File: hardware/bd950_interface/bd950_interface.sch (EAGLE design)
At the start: 16 parts, among them IC1 FT4232HL, IC2 MAX208ECWG, IC3 4050D, X1 ECG.0B.304.CLV

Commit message: Continue work on BD950 interface board
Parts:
- added C1, C2, C3: 3.3uF, resistor:C-USC0603
- added IC4: AT93C46A-10SQ-2.7, atmel:AT93C46A-10SQ-2.7
- added Q1: (no value), adafruit:CRYSTALHC49S
- added R10: 2.2k, resistor:R-US_R0603
- added R11, R6: 12k, resistor:R-US_R0603
- added R7, R8, R9: 10k, resistor:R-US_R0603
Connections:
- new net +3V3: IC1CORE.VCCIO@1, IC1CORE.VCCIO@2, IC1CORE.VCCIO@3, IC1CORE.VCCIO@4, IC1CORE.VPHY, IC1CORE.VPLL, IC1CORE.VREGIN, IC4.VCC, R11.2, R7.2, R8.2, R9.2
- new net EECLK: IC1CORE.EECLK, IC4.SK, R8.1
- new net EECS: IC1CORE.EECS, IC4.CS, R9.1
- new net EEDATA: IC1CORE.EEDATA, IC4.DI, R10.2
- new net N$10: C1.1, IC1CORE.VCORE@1, IC1CORE.VCORE@2, IC1CORE.VCORE@3, IC1CORE.VREGOUT
- new net N$11: C3.1, IC1CORE.XTOUT, Q1.1
- new net N$12: C2.1, IC1CORE.XTIN, Q1.2
- new net N$13: IC1CORE.RESET#, R11.1
- new net N$6: IC1CORE.REF, R6.2
- new net N$9: IC4.DO, R10.1, R7.1
- new net UART1_RXD: IC1A.DB1/RXD, IC2G$1.R1OUT
- new net UART1_TXD: IC1A.DB0/TXD, IC2G$1.T1IN
- new net UART2_RXD: IC1B.DB1/RXD, IC2G$1.R2OUT
- new net UART2_TXD: IC1B.DB0/TXD, IC2G$1.T2IN
- new net UART3_RXD: IC2G$1.R3OUT
- new net UART3_TXD: IC1C.DB0/TXD, IC1C.DB1/RXD, IC2G$1.T3IN
- new net UART4_RXD: IC1D.DB1/RXD, IC2G$1.R4OUT, IC2G$1.T4IN
- new net UART4_TXD: IC1D.DB0/TXD
- net 1PPS_PORT1: now also IC1A.DB6/DCD
- net 1PPS_PORT2: now also IC1B.DB6/DCD
- net 1PPS_PORT3: now also IC1C.DB6/DCD
- net 1PPS_PORT4: now also IC1D.DB6/DCD
- net GND: now also C1.2, C2.2, C3.2, IC1CORE.TEST, IC4.GND, R6.1
- net PORT1_RXD: now also IC2G$1.T1OUT
- net PORT2_RXD: now also IC2G$1.T2OUT
- net PORT3_RXD: now also IC2G$1.T3OUT
- net PORT4_RXD: now also IC2G$1.T4OUT
- net PORT4_TXD: now also IC2G$1.R1IN, IC2G$1.R2IN, IC2G$1.R3IN, IC2G$1.R4IN
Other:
- note added: "Most of this is copied verbatim from the FTDI AN, Figure 6.1"
- note added: "USB Serial Converter"
- note removed: "Connectors"
- moved on the sheet: IC1A, IC1B, IC1C, IC1D, IC2

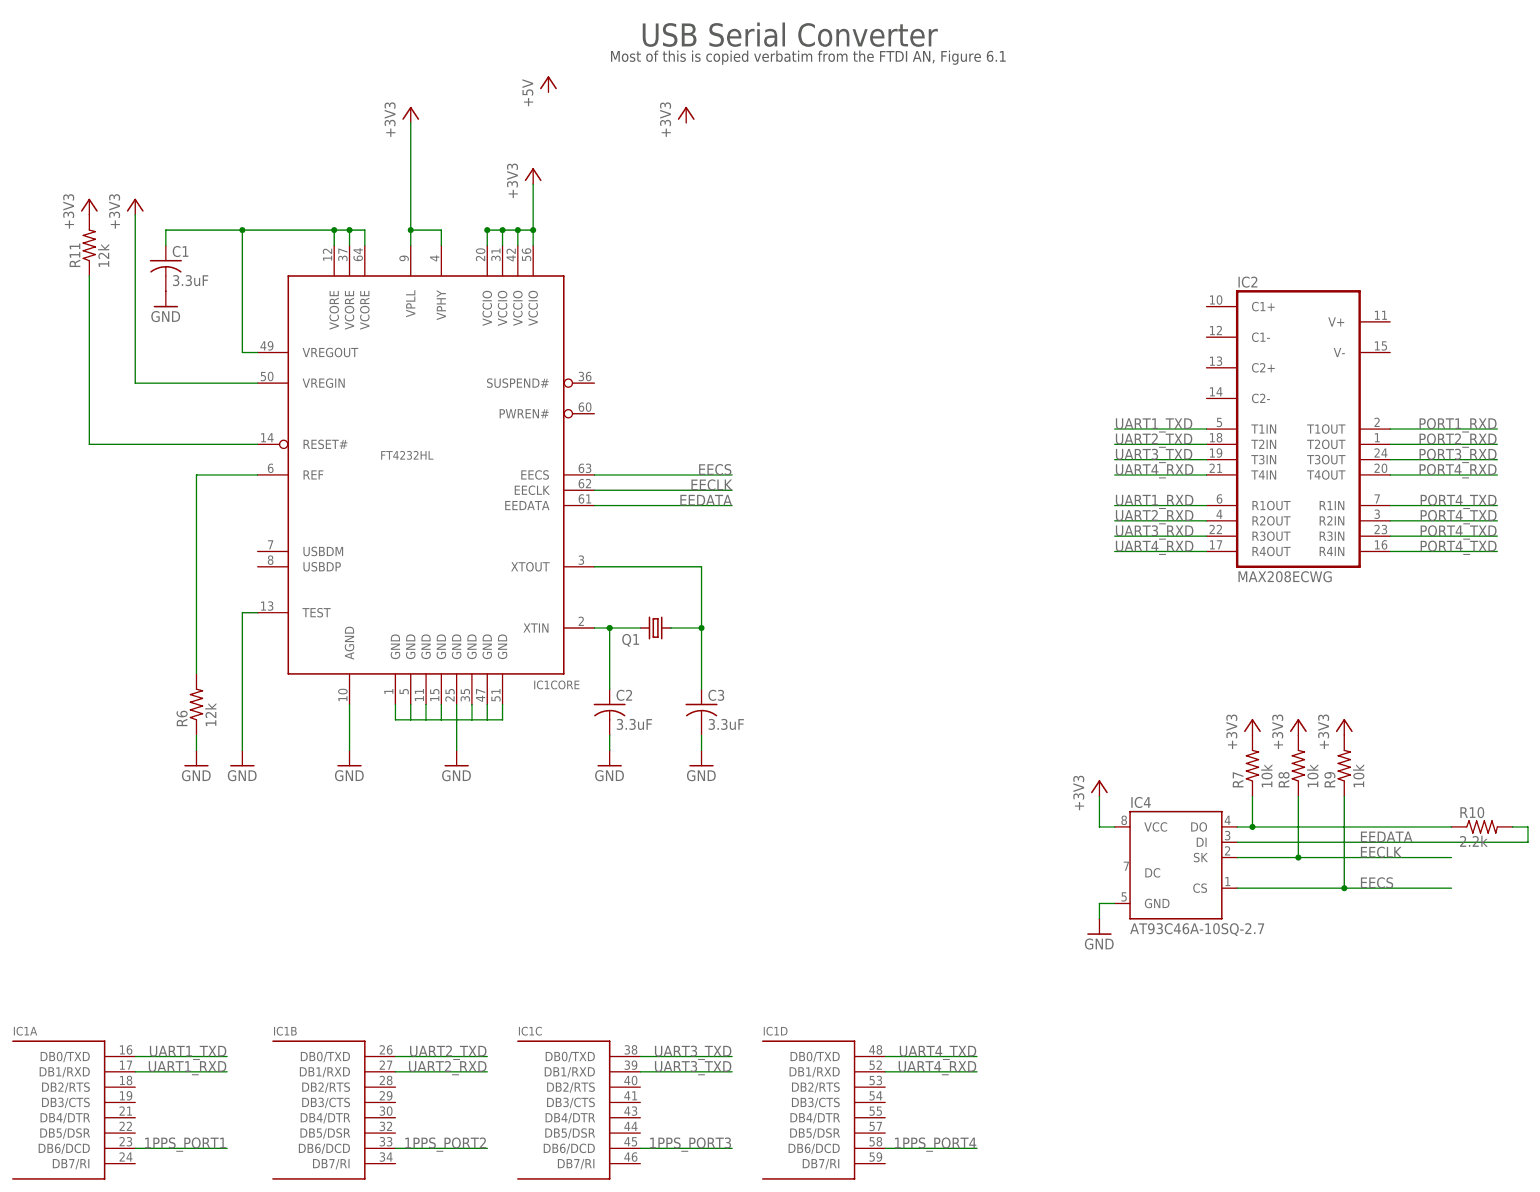
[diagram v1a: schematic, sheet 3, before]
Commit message: Make BD950 interface board USB powered
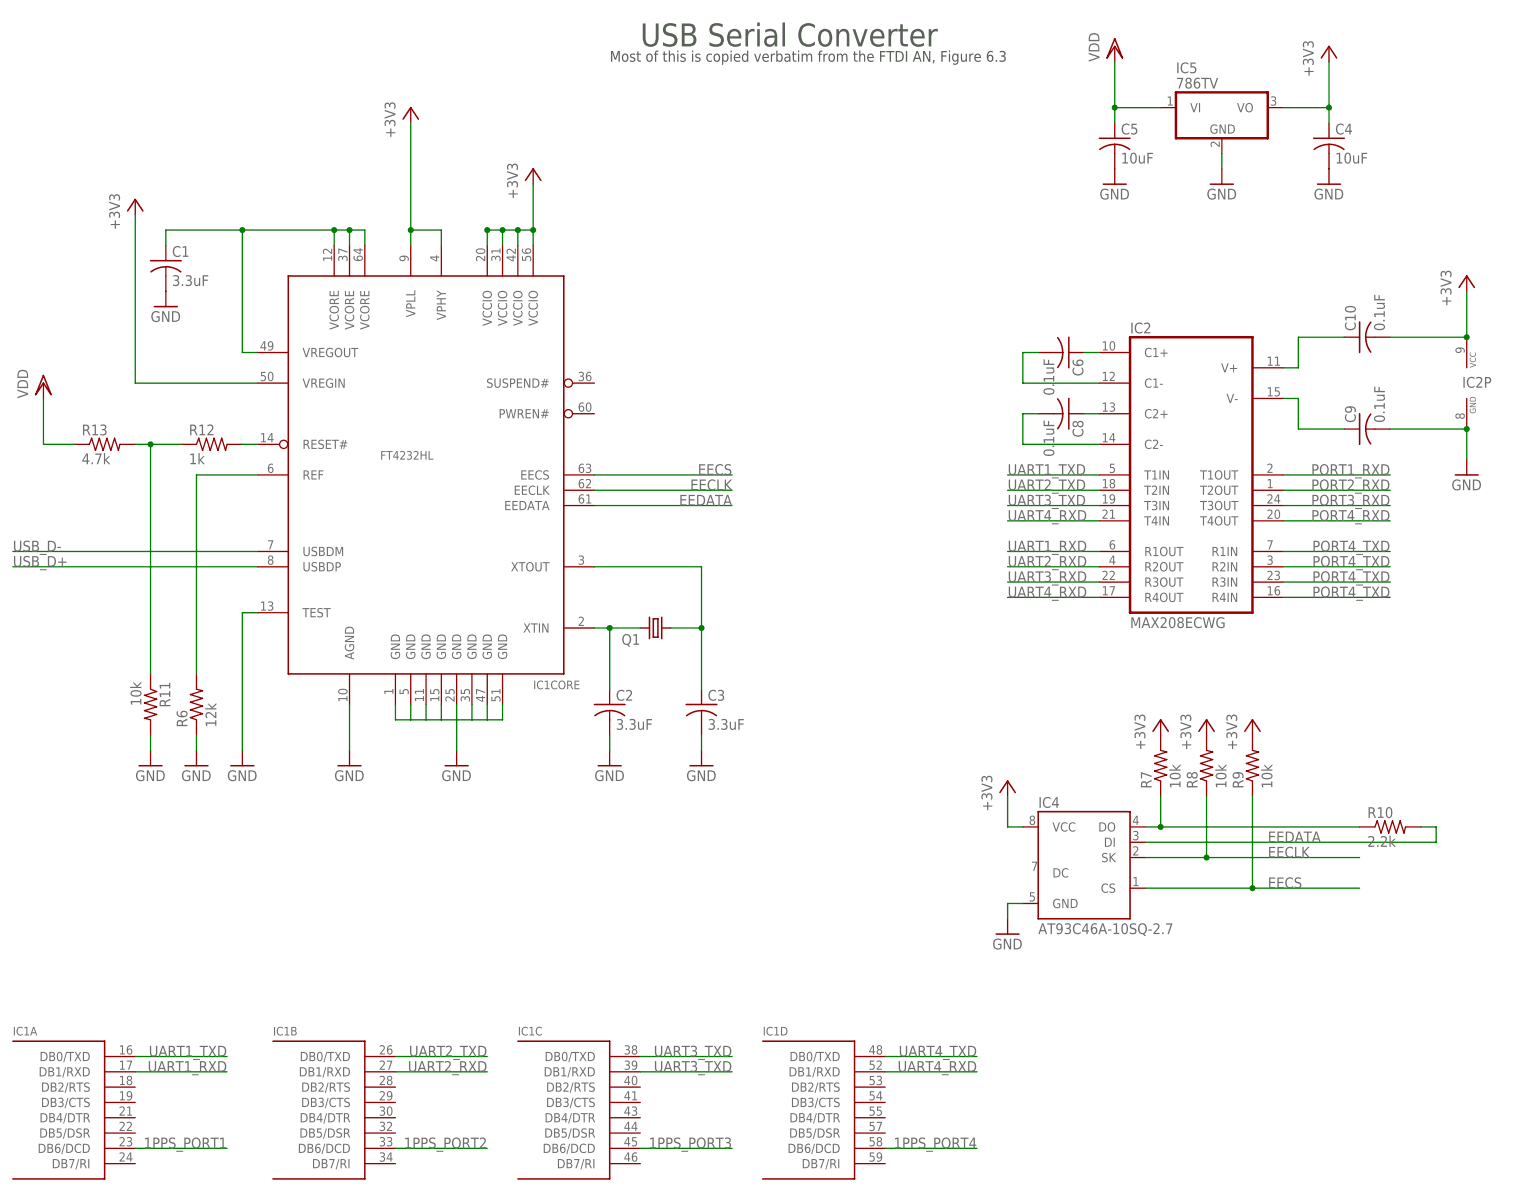
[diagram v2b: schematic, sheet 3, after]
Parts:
- removed D7: BAT60J, diode:BAT60J
- added C10, C6, C8, C9: 0.1uF, resistor:C-USC0603
- added C4, C5: 10uF, resistor:C-USC0603
- added IC5: 786TV, linear:786TV
- added R12: 1k, resistor:R-US_R0603
- added R13: 4.7k, resistor:R-US_R0603
- added U$1: MUSBB15130, adafruit:MUSBB15130
- R11: value 12k -> 10k
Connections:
- removed net V+: C7.1, D7.C, U$2.VIN@0, U$2.VIN@1
- new net N$14: C6.1, IC2G$1.C1+
- new net N$15: IC1CORE.RESET#, R12.2
- new net N$16: C6.2, IC2G$1.C1-
- new net N$17: C8.1, IC2G$1.C2+
- new net N$18: C8.2, IC2G$1.C2-
- new net N$19: C9.1, IC2G$1.V-
- new net N$20: C10.1, IC2G$1.V+
- new net USB_D+: IC1CORE.USBDP, U$1.D+
- new net USB_D-: IC1CORE.USBDM, U$1.D-
- new net VDD: C7.1, R13.1, U$1.VBUS, U$2.VIN@0, U$2.VIN@1
- net +3V3: now also C10.2, C4.1, IC2P.VCC, IC3P.VDD, IC5.VO; no longer R11.2
- net GND: now also C4.2, C5.2, C9.2, IC2P.GND, IC3P.VSS, IC5.GND, R11.2, U$1.GND, X1.4
- net N$13: now also R12.1, R13.2; no longer IC1CORE.RESET#
- net N$2: now also C5.1, IC5.VI; no longer D7.A
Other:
- note added: "Most of this is copied verbatim from the FTDI AN, Figure 6.3"
- note removed: "Most of this is copied verbatim from the FTDI AN, Figure 6.1"
- moved on the sheet: IC2, IC4, R10, R11, R7, R8, R9

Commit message: Continue laying out BD950 interface board
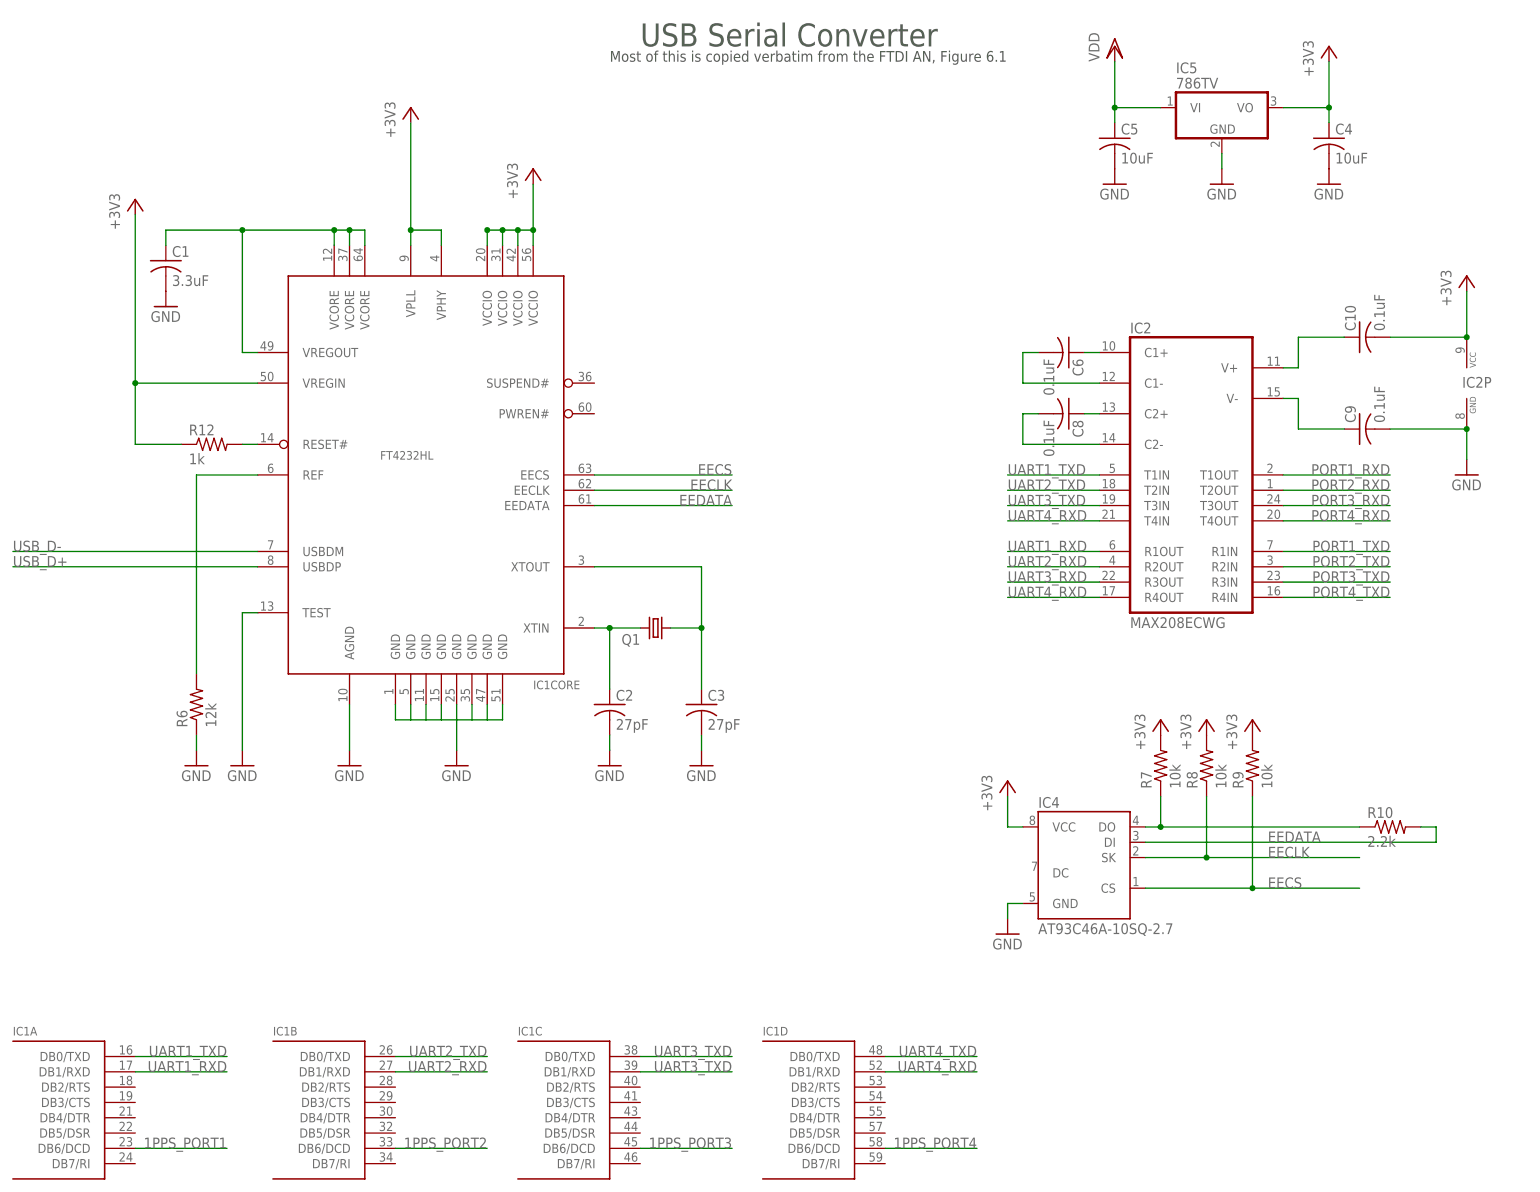
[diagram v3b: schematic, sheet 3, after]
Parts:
- removed R11: 10k, resistor:R-US_R0603
- removed R13: 4.7k, resistor:R-US_R0603
- C2, C3: value 3.3uF -> 27pF
- LED1, LED2, LED3: device adafruit:LED5MM -> adafruit:LEDCHIP-LED0603
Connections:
- removed net N$13: R11.1, R12.1, R13.2
- net +3V3: now also R12.1
- net GND: no longer R11.2
- net PORT1_TXD: now also IC2G$1.R1IN
- net PORT2_TXD: now also IC2G$1.R2IN
- net PORT3_TXD: now also IC2G$1.R3IN
- net PORT4_TXD: no longer IC2G$1.R1IN, IC2G$1.R2IN, IC2G$1.R3IN
- net VDD: no longer R13.1
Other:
- note added: "Most of this is copied verbatim from the FTDI AN, Figure 6.1"
- note removed: "Most of this is copied verbatim from the FTDI AN, Figure 6.3"
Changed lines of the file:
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@@
 <part name="C7" library="resistor" deviceset="C-US" device="C0805" value="4.7uF"/>
 <part name="GND35" library="supply1" deviceset="GND" device=""/>
-<part name="LED3" library="adafruit" deviceset="LED" device="5MM" value="SSF-LXH103UWC"/>
+<part name="LED3" library="adafruit" deviceset="LED" device="CHIP-LED0603" value="SSF-LXH103UWC"/>
 <part name="R19" library="rcl" deviceset="R-US_" device="R0603" value="10k"/>
 <part name="GND38" library="supply1" deviceset="GND" device=""/>
@@
 <part name="R1" library="rcl" deviceset="R-US_" device="R0603" value="0"/>
 <part name="GND4" library="supply1" deviceset="GND" device=""/>
-<part name="LED1" library="adafruit" deviceset="LED" device="5MM" value="SSF-LXH103UWC"/>
+<part name="LED1" library="adafruit" deviceset="LED" device="CHIP-LED0603" value="SSF-LXH103UWC"/>
 <part name="R2" library="rcl" deviceset="R-US_" device="R0603" value="10k"/>
 <part name="GND5" library="supply1" deviceset="GND" device=""/>
-<part name="LED2" library="adafruit" deviceset="LED" device="5MM" value="SSF-LXH103UWC"/>
+<part name="LED2" library="adafruit" deviceset="LED" device="CHIP-LED0603" value="SSF-LXH103UWC"/>
 <part name="R3" library="rcl" deviceset="R-US_" device="R0603" value="10k"/>
 <part name="GND6" library="supply1" deviceset="GND" device=""/>
@@
 <part name="R10" library="resistor" deviceset="R-US_" device="R0603" value="2.2k"/>
 <part name="Q1" library="adafruit" deviceset="CRYSTAL" device="HC49S"/>
-<part name="C2" library="resistor" deviceset="C-US" device="C0603" value="3.3uF"/>
-<part name="C3" library="resistor" deviceset="C-US" device="C0603" value="3.3uF"/>
+<part name="C2" library="resistor" deviceset="C-US" device="C0603" value="27pF"/>
+<part name="C3" library="resistor" deviceset="C-US" device="C0603" value="27pF"/>
 <part name="GND12" library="supply1" deviceset="GND" device=""/>
 <part name="GND13" library="supply1" deviceset="GND" device=""/>
-<part name="R11" library="resistor" deviceset="R-US_" device="R0603" value="10k"/>
 <part name="+3V6" library="supply1" deviceset="+3V3" device=""/>
 <part name="GND14" library="supply1" deviceset="GND" device=""/>
@@
 <part name="C5" library="resistor" deviceset="C-US" device="C0603" value="10uF"/>
 <part name="GND17" library="supply1" deviceset="GND" device=""/>
-<part name="GND18" library="supply1" deviceset="GND" device=""/>
 <part name="R12" library="resistor" deviceset="R-US_" device="R0603" value="1k"/>
 <part name="U$1" library="adafruit" deviceset="MUSBB15130" device=""/>
@@
 <part name="VDD3" library="supply1" deviceset="VDD" device=""/>
 <part name="VDD4" library="supply1" deviceset="VDD" device=""/>
-<part name="R13" library="resistor" deviceset="R-US_" device="R0603" value="4.7k"/>
-<part name="VDD5" library="supply1" deviceset="VDD" device=""/>
 <part name="C6" library="resistor" deviceset="C-US" device="C0603" value="0.1uF"/>
 <part name="C8" library="resistor" deviceset="C-US" device="C0603" value="0.1uF"/>
@@
 <plain>
 <text x="114.3" y="203.2" size="3.81" layer="97">USB Serial Converter</text>
-<text x="109.22" y="200.66" size="1.778" layer="97">Most of this is copied verbatim from the FTDI AN, Figure 6.3</text>
+<text x="109.22" y="200.66" size="1.778" layer="97">Most of this is copied verbatim from the FTDI AN, Figure 6.1</text>
 </plain>
 <instances>
@@
 <instance part="GND12" gate="1" x="109.22" y="83.82"/>
 <instance part="GND13" gate="1" x="124.46" y="83.82"/>
-<instance part="R11" gate="G$1" x="33.02" y="93.98" rot="R270"/>
 <instance part="+3V6" gate="G$1" x="30.48" y="177.8"/>
 <instance part="GND14" gate="1" x="48.26" y="83.82"/>
@@
 <instance part="C5" gate="G$1" x="193.04" y="187.96"/>
 <instance part="GND17" gate="1" x="193.04" y="180.34"/>
-<instance part="GND18" gate="1" x="33.02" y="83.82"/>
 <instance part="R12" gate="G$1" x="43.18" y="137.16"/>
 <instance part="VDD4" gate="G$1" x="193.04" y="203.2"/>
-<instance part="R13" gate="G$1" x="25.4" y="137.16"/>
-<instance part="VDD5" gate="G$1" x="15.24" y="147.32"/>
 <instance part="C6" gate="G$1" x="185.42" y="152.4" rot="R270"/>
 <instance part="C8" gate="G$1" x="185.42" y="142.24" rot="R270"/>
@@
 </segment>
 <segment>
-<pinref part="R11" gate="G$1" pin="2"/>
-<pinref part="GND18" gate="1" pin="GND"/>
-<wire x1="33.02" y1="88.9" x2="33.02" y2="86.36" width="0.1524" layer="91"/>
-</segment>
-<segment>
 <pinref part="C9" gate="G$1" pin="2"/>
 <pinref part="GND20" gate="1" pin="GND"/>
@@
 </net>
 <net name="PORT4_TXD" class="0">
-<segment>
-<pinref part="IC2" gate="G$1" pin="R1IN"/>
-<wire x1="220.98" y1="119.38" x2="238.76" y2="119.38" width="0.1524" layer="91"/>
-<label x="238.76" y="119.38" size="1.778" layer="95" rot="MR0"/>
-</segment>
-<segment>
-<pinref part="IC2" gate="G$1" pin="R2IN"/>
-<wire x1="220.98" y1="116.84" x2="238.76" y2="116.84" width="0.1524" layer="91"/>
-<label x="238.76" y="116.84" size="1.778" layer="95" rot="MR0"/>
-</segment>
-<segment>
-<pinref part="IC2" gate="G$1" pin="R3IN"/>
-<wire x1="220.98" y1="114.3" x2="238.76" y2="114.3" width="0.1524" layer="91"/>
-<label x="238.76" y="114.3" size="1.778" layer="95" rot="MR0"/>
-</segment>
 <segment>
 <pinref part="IC2" gate="G$1" pin="R4IN"/>
@@
 <wire x1="50.8" y1="147.32" x2="30.48" y2="147.32" width="0.1524" layer="91"/>
 <wire x1="30.48" y1="147.32" x2="30.48" y2="175.26" width="0.1524" layer="91"/>
+<pinref part="R12" gate="G$1" pin="1"/>
+<wire x1="38.1" y1="137.16" x2="30.48" y2="137.16" width="0.1524" layer="91"/>
+<wire x1="30.48" y1="137.16" x2="30.48" y2="147.32" width="0.1524" layer="91"/>
+<junction x="30.48" y="147.32"/>
 </segment>
 <segment>
@@
 </segment>
 </net>
-<net name="N$13" class="0">
-<segment>
-<pinref part="R11" gate="G$1" pin="1"/>
-<wire x1="33.02" y1="137.16" x2="33.02" y2="99.06" width="0.1524" layer="91"/>
-<pinref part="R12" gate="G$1" pin="1"/>
-<wire x1="38.1" y1="137.16" x2="33.02" y2="137.16" width="0.1524" layer="91"/>
-<pinref part="R13" gate="G$1" pin="2"/>
-<wire x1="30.48" y1="137.16" x2="33.02" y2="137.16" width="0.1524" layer="91"/>
-<junction x="33.02" y="137.16"/>
-</segment>
-</net>
 <net name="N$15" class="0">
 <segment>
@@
 </segment>
 </net>
-<net name="VDD" class="0">
-<segment>
-<pinref part="VDD5" gate="G$1" pin="VDD"/>
-<wire x1="15.24" y1="144.78" x2="15.24" y2="137.16" width="0.1524" layer="91"/>
-<pinref part="R13" gate="G$1" pin="1"/>
-<wire x1="15.24" y1="137.16" x2="20.32" y2="137.16" width="0.1524" layer="91"/>
-</segment>
-</net>
 <net name="N$16" class="0">
 <segment>
@@
 </segment>
 </net>
+<net name="PORT1_TXD" class="0">
+<segment>
+<pinref part="IC2" gate="G$1" pin="R1IN"/>
+<wire x1="220.98" y1="119.38" x2="238.76" y2="119.38" width="0.1524" layer="91"/>
+<label x="238.76" y="119.38" size="1.778" layer="95" rot="MR0"/>
+</segment>
+</net>
+<net name="PORT2_TXD" class="0">
+<segment>
+<pinref part="IC2" gate="G$1" pin="R2IN"/>
+<wire x1="220.98" y1="116.84" x2="238.76" y2="116.84" width="0.1524" layer="91"/>
+<label x="238.76" y="116.84" size="1.778" layer="95" rot="MR0"/>
+</segment>
+</net>
+<net name="PORT3_TXD" class="0">
+<segment>
+<pinref part="IC2" gate="G$1" pin="R3IN"/>
+<wire x1="220.98" y1="114.3" x2="238.76" y2="114.3" width="0.1524" layer="91"/>
+<label x="238.76" y="114.3" size="1.778" layer="95" rot="MR0"/>
+</segment>
+</net>
